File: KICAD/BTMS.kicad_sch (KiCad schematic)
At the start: 140 parts, among them J1 Batt_Ballance, J2 AUX_Charge, J3 Battery_IO, J4 Power_Out, J5 BTemp, J6 DSKY, J7 PWR_SW, J8 ICSP, J9 Heater, P1 USB_C_Plug, Q1 SSM3K341R, Q2 DMN65D8L, Q3 SSM3K341R, Q4 FDN340P, Q5 FDN340P, Q6 FDN340P, Q7 DMN65D8L, Q8 DMN65D8L, U1 ACS711xLCTR-25AB, U10 BA033CC0FP-E2, U11 AON7522E, U12 AON7522E, U13 LM62CIM3/NOPB, U14 FAN3100TSX, U15 FAN3100TSX, U16 AON7522E, U17 dsPIC30F3011-PT, U18 FT230XQ, U2 AP33771, U3 IS281-4, U4 Q294700DSGR, U5 SCF4030-12-0X, U6 AONR21321, U7 ACS711xLCTR-25AB, U8 IS281-4, U9 IRS2184

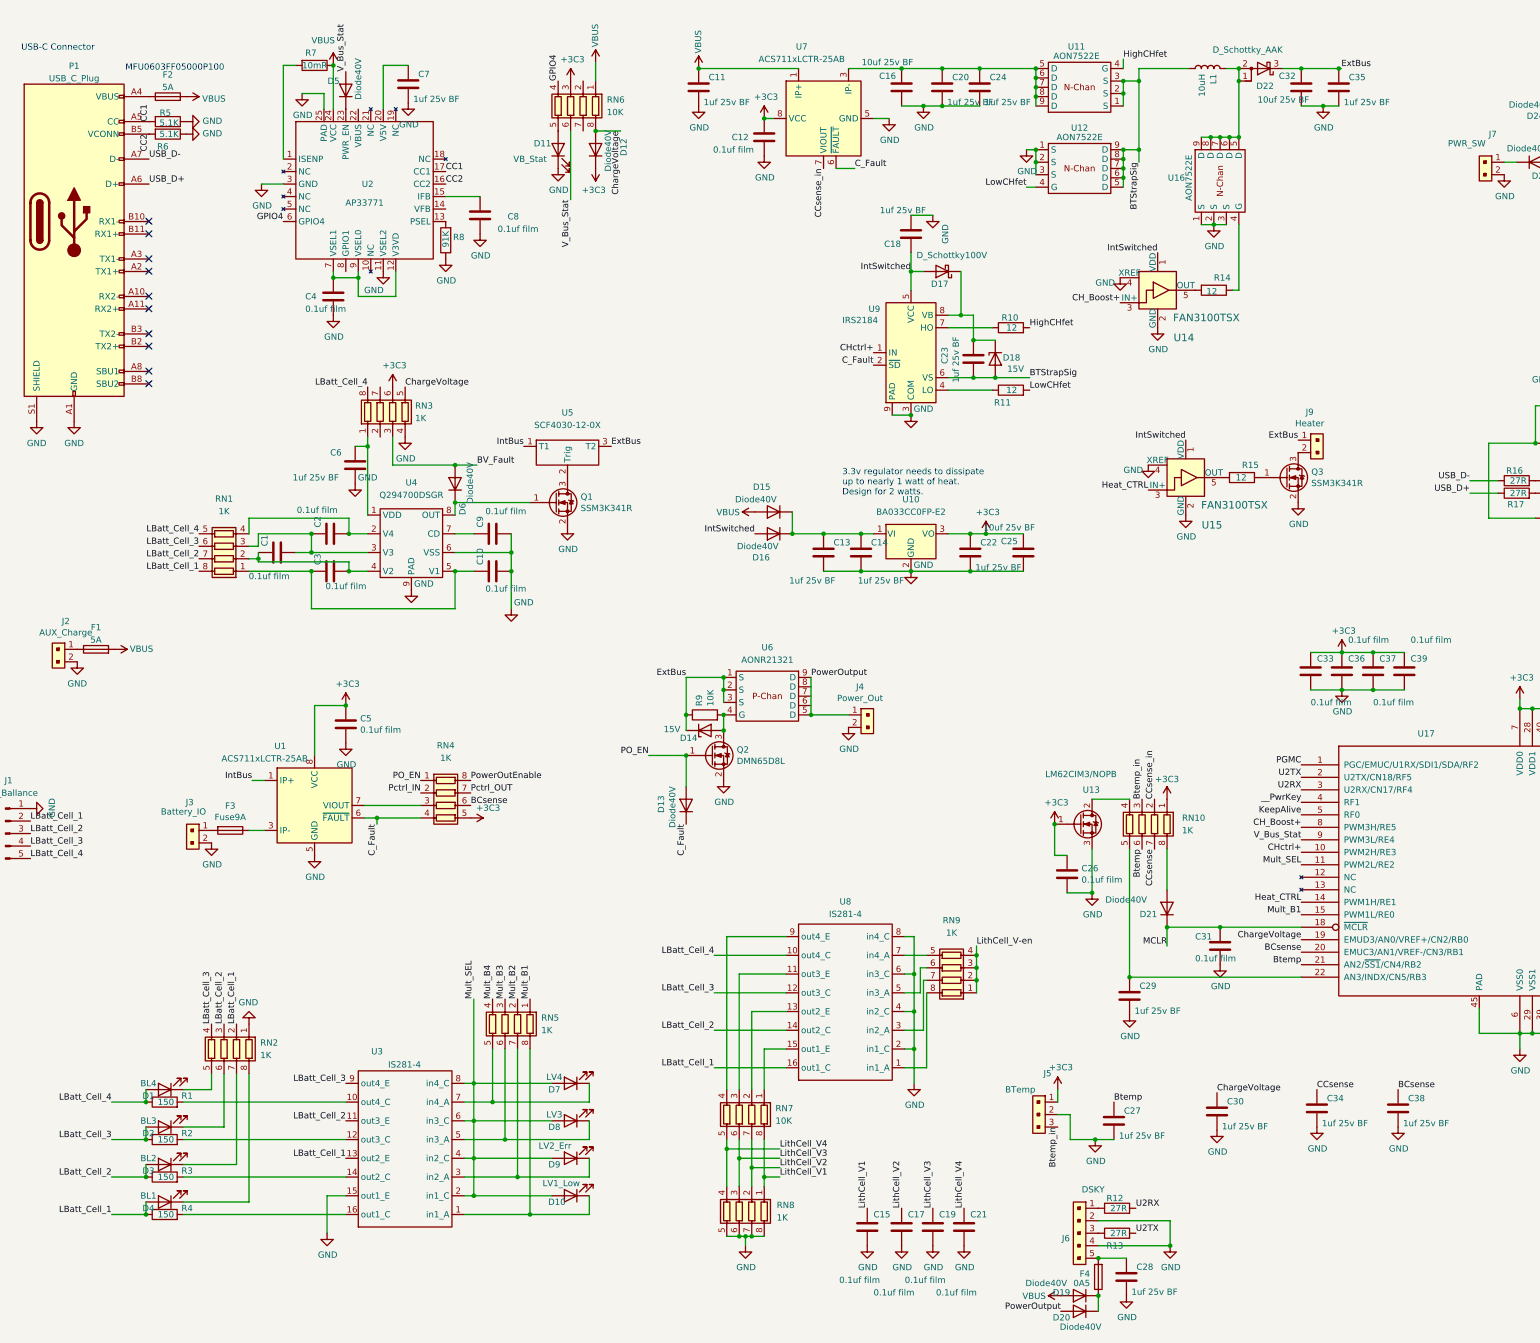
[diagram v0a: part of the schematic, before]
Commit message: Started running traces.
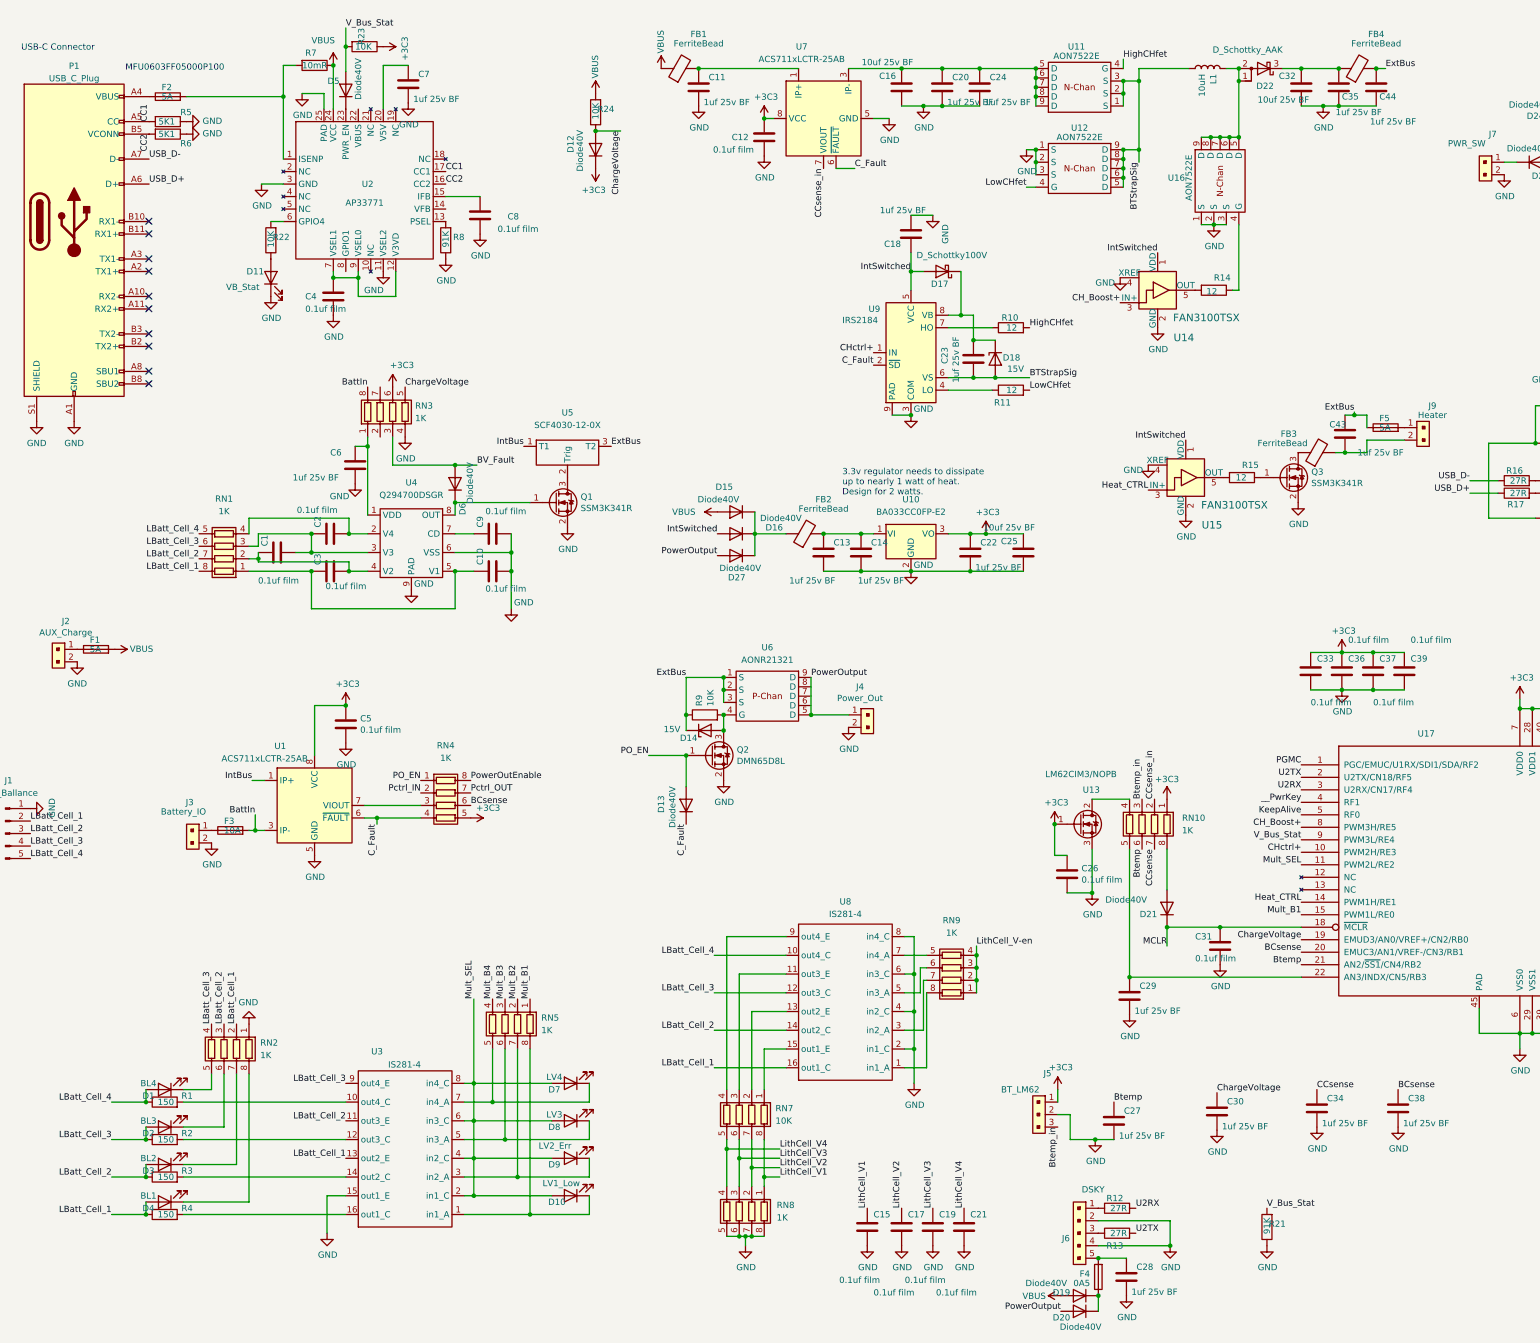
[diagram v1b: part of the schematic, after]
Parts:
- removed RN6: 10K, Resistor_SMD:R_Array_Convex_4x1206, symbol Device:R_Pack04
- added C43, C44: 1uf 25v BF, Capacitor_SMD:C_0603_1608Metric, symbol Device:C
- added D27: Diode40V, Diode_SMD:D_0603_1608Metric, symbol Device:D
- added F5: 5A, Fuse:Fuse_1206_3216Metric, symbol Device:Fuse
- added FB1, FB2, FB3, FB4: FerriteBead, Resistor_SMD:R_1206_3216Metric, symbol Device:FerriteBead
- added R21: 91K, Resistor_SMD:R_0603_1608Metric, symbol Device:R
- added R22, R23, R24: 10K, Resistor_SMD:R_0603_1608Metric, symbol Device:R
- F1, F2: footprint Fuse:Fuse_0603_1608Metric_Pad1.05x0.95mm_HandSolder -> Fuse:Fuse_1206_3216Metric; DK_Detail_Page (none) -> https://www.digikey.com/en/products/detail/bel-fuse-inc/C1F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; Digi-Key_PN (none) -> 507-1886-1-ND
- F3: value Fuse9A -> 10A; footprint Fuse:Fuse_0603_1608Metric_Pad1.05x0.95mm_HandSolder -> Fuse:Fuse_1206_3216Metric; DK_Detail_Page (none) -> https://www.digikey.com/en/products/detail/bel-fuse-inc/068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; Digi-Key_PN (none) -> 507-1942-1-ND
- F4: DK_Detail_Page (none) -> https://www.digikey.com/en/products/detail/bel-fuse-inc/C2Q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; Digi-Key_PN (none) -> 507-1089-1-ND
- J5: value BTemp -> BT_LM62
- R5, R6: value 5.1K -> 5K1; DK_Detail_Page (none) -> https://www.digikey.com/en/products/detail/yageo/RC0603FR-1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; Digi-Key_PN (none) -> 13-RC0603FR-135K1LCT-ND
- R7: footprint Resistor_SMD:R_0603_1608Metric -> Resistor_SMD:R_1206_3216Metric; DK_Detail_Page (none) -> https://www.digikey.com/en/products/detail/stackpole-electr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; Digi-Key_PN (none) -> CSR1206FT10L0CT-ND
- R8: DK_Detail_Page (none) -> https://www.digikey.com/en/products/detail/stackpole-electr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; Digi-Key_PN (none) -> RMCF0603FT91K0CT-ND
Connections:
- net +5C: now also R23.1
- net ChargeVoltage: now also R24.1
- net ExtBus: now also C43.1, C44.1, F5.1, FB4.2; no longer C32.1, C35.1, D22.3 (K), J9.1
- net GND: now also C44.2, R21.1
- net LBatt_Cell_4: no longer RN3.8 (R1.2)
- net PowerOutput: now also D27.2 (A)
- net VBUS: now also FB1.1, R24.2; no longer C11.1, F2.2, U7.1 (IP+), U7.2 (IP+)
- net V_Bus_Stat: now also R21.2, R23.2
- net at J9.2: now also C43.2, FB3.2; no longer Q3.3 (D)
- net at C13.1, C14.1, U10.1 (VI): now also FB2.2; no longer D15.1 (K), D16.1 (K)
- net at J3.1: now also F3.1; no longer F3.2
- net BattIn: now reaches U1.3 (IP-), U1.4 (IP-)
- net BattIn: now also F3.2, RN3.8 (R1.2); no longer F3.1
- net at R7.2, U2.1 (ISENP): now also F2.2
- net at D11.2 (A): now also R22.1
- net GPIO4: no longer names the net of U2.6 (GPIO4)
- net GPIO4: now also R22.2
- new net: C32.1, C35.1, D22.3 (K), FB4.1
- new net: C11.1, FB1.2, U7.1 (IP+), U7.2 (IP+)
- new net: D15.1 (K), D16.1 (K), D27.1 (K), FB2.1
- new net: F5.2, J9.1
- new net: FB3.1, Q3.3 (D)
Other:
- moved on the sheet: D11, D15, D16, J9

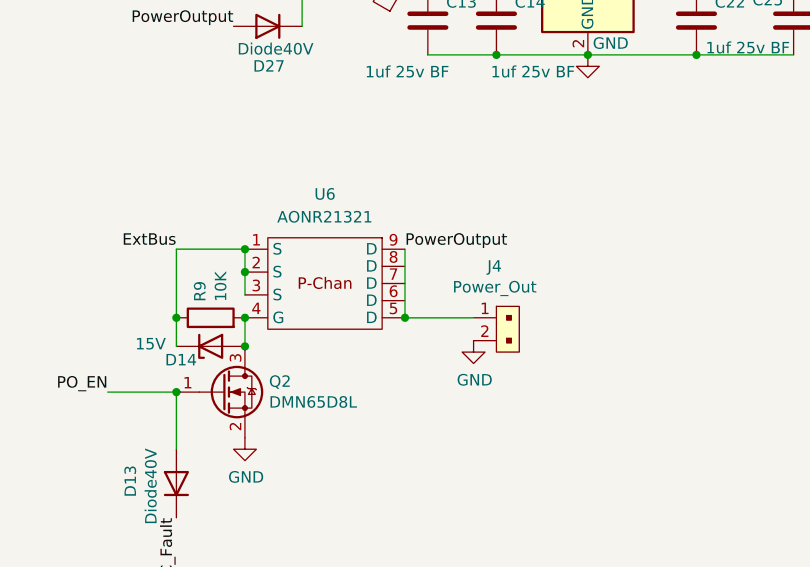
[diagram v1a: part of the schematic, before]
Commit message: Board routing complete and cleaned up all board DRV violations except some silkscreen warning on the bottom edge.
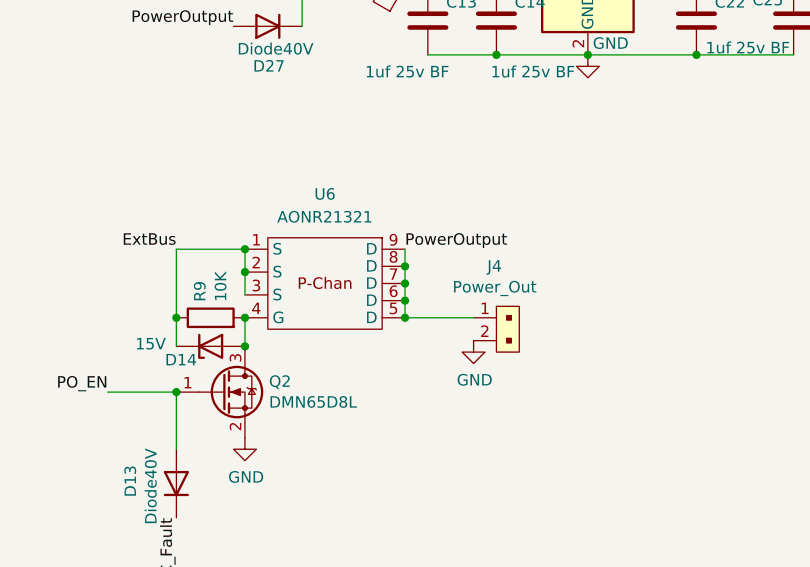
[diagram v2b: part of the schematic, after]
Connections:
- net PowerOutput: now also U6.6 (D), U6.7 (D), U6.8 (D)
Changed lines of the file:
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@@
   (junction (at 267.97 200.025) (diameter 0) (color 0 0 0 0)
   )
+  (junction (at 122.555 243.205) (diameter 0) (color 0 0 0 0)
+  )
+  (junction (at 194.945 120.015) (diameter 0) (color 0 0 0 0)
+  )
+  (junction (at 161.925 25.4) (diameter 0) (color 0 0 0 0)
+  )
+  (junction (at 167.005 156.845) (diameter 0) (color 0 0 0 0)
+  )
+  (junction (at 299.085 151.765) (diameter 0) (color 0 0 0 0)
+  )
+  (junction (at 94.615 102.235) (diameter 0) (color 0 0 0 0)
+  )
+  (junction (at 77.47 31.115) (diameter 0) (color 0 0 0 0)
+  )
+  (junction (at 215.265 75.565) (diameter 0) (color 0 0 0 0)
+  )
   (junction (at 184.785 156.845) (diameter 0) (color 0 0 0 0)
   )
-  (junction (at 122.555 243.205) (diameter 0) (color 0 0 0 0)
-  )
-  (junction (at 194.945 120.015) (diameter 0) (color 0 0 0 0)
-  )
-  (junction (at 161.925 25.4) (diameter 0) (color 0 0 0 0)
-  )
-  (junction (at 167.005 156.845) (diameter 0) (color 0 0 0 0)
-  )
-  (junction (at 299.085 151.765) (diameter 0) (color 0 0 0 0)
-  )
-  (junction (at 94.615 102.235) (diameter 0) (color 0 0 0 0)
-  )
-  (junction (at 77.47 31.115) (diameter 0) (color 0 0 0 0)
-  )
-  (junction (at 215.265 75.565) (diameter 0) (color 0 0 0 0)
-  )
   (junction (at 344.805 44.45) (diameter 0) (color 0 0 0 0)
   )
@@
   (junction (at 83.185 123.825) (diameter 0) (color 0 0 0 0)
   )
+  (junction (at 184.785 153.035) (diameter 0) (color 0 0 0 0)
+  )
   (junction (at 83.185 120.015) (diameter 0) (color 0 0 0 0)
   )
@@
   )
   (junction (at 159.385 156.845) (diameter 0) (color 0 0 0 0)
+  )
+  (junction (at 184.785 151.13) (diameter 0) (color 0 0 0 0)
+  )
+  (junction (at 184.785 154.94) (diameter 0) (color 0 0 0 0)
   )
   (junction (at 218.44 210.82) (diameter 0) (color 0 0 0 0)
@@
     (stroke (width 0) (type default) (color 0 0 0 0))
   )
+  (wire (pts (xy 184.785 149.225) (xy 184.785 151.13))
+    (stroke (width 0) (type default) (color 0 0 0 0))
+  )
   (wire (pts (xy 70.485 255.905) (xy 57.15 255.905))
     (stroke (width 0) (type default) (color 0 0 0 0))
@@
     (stroke (width 0) (type default) (color 0 0 0 0))
   )
+  (wire (pts (xy 184.785 154.94) (xy 184.785 156.845))
+    (stroke (width 0) (type default) (color 0 0 0 0))
+  )
   (wire (pts (xy 194.945 127.635) (xy 205.105 127.635))
     (stroke (width 0) (type default) (color 0 0 0 0))
@@
     (stroke (width 0) (type default) (color 0 0 0 0))
   )
+  (wire (pts (xy 184.785 151.13) (xy 184.785 153.035))
+    (stroke (width 0) (type default) (color 0 0 0 0))
+  )
   (wire (pts (xy 175.26 250.825) (xy 178.435 250.825))
     (stroke (width 0) (type default) (color 0 0 0 0))
@@
     (stroke (width 0) (type default) (color 0 0 0 0))
   )
-  (wire (pts (xy 184.785 149.225) (xy 184.785 156.845))
-    (stroke (width 0) (type default) (color 0 0 0 0))
-  )
   (wire (pts (xy 125.095 250.825) (xy 114.3 250.825))
     (stroke (width 0) (type default) (color 0 0 0 0))
@@
     (stroke (width 0) (type default) (color 0 0 0 0))
   )
+  (wire (pts (xy 184.785 153.035) (xy 184.785 154.94))
+    (stroke (width 0) (type default) (color 0 0 0 0))
+  )
